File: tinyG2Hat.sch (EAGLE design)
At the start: 31 parts

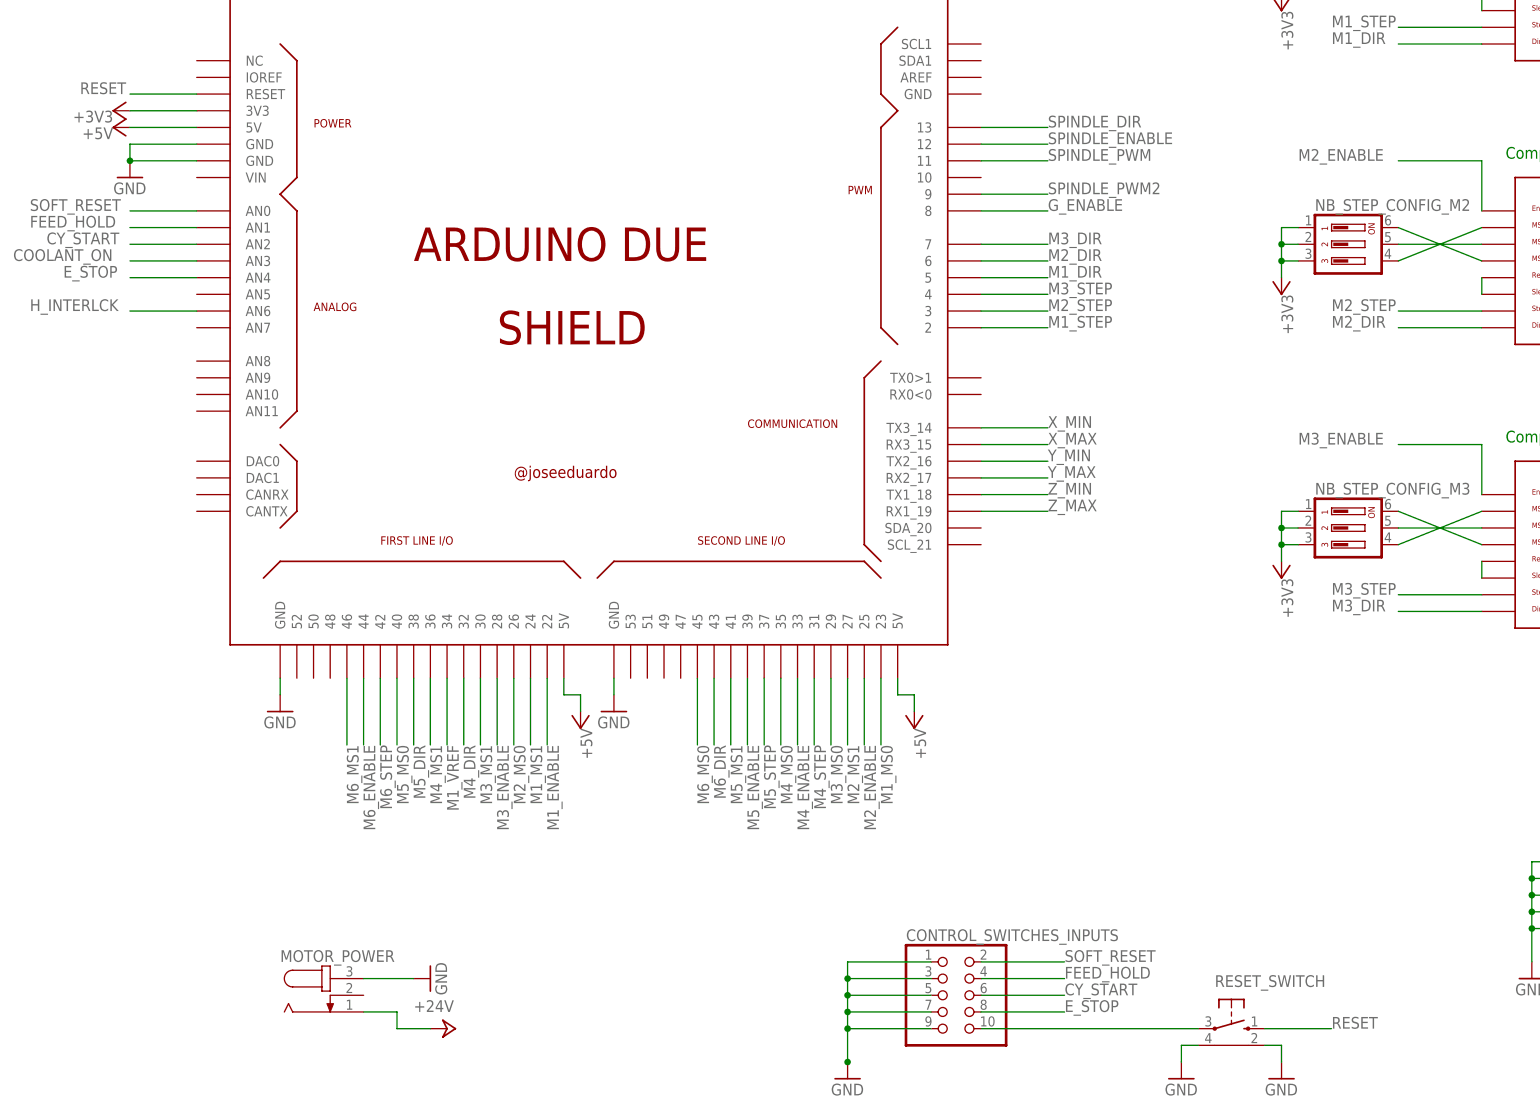
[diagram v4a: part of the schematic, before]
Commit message: Routage de base terminé
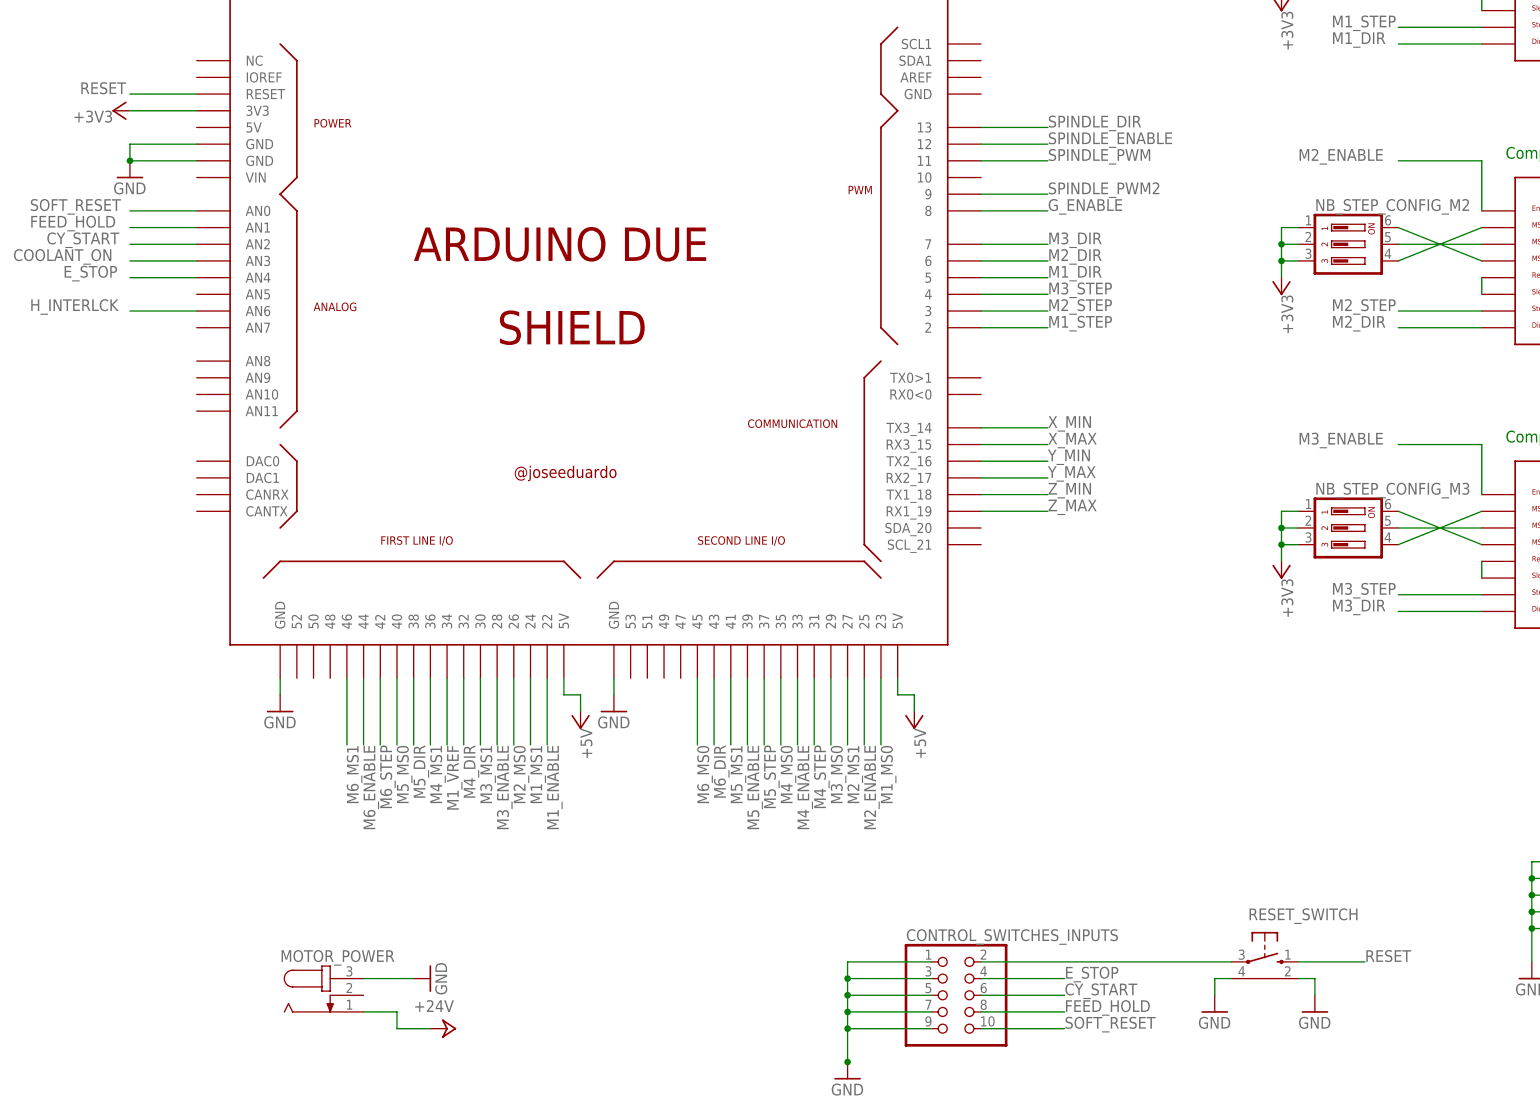
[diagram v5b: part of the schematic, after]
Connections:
- net +5V: no longer ARDUINO_DUE1.5V
- net E_STOP: now also CONTROL_SWITCHES_INPUTS.4; no longer CONTROL_SWITCHES_INPUTS.8
- net FEED_HOLD: now also CONTROL_SWITCHES_INPUTS.8; no longer CONTROL_SWITCHES_INPUTS.4
- net N$50: now also CONTROL_SWITCHES_INPUTS.2; no longer CONTROL_SWITCHES_INPUTS.10
- net SOFT_RESET: now also CONTROL_SWITCHES_INPUTS.10; no longer CONTROL_SWITCHES_INPUTS.2
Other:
- moved on the sheet: RESET_SWITCH
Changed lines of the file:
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@@
 <part name="ARDUINO_DUE1" library="arduino_due_shield" deviceset="ARDUINO_DUE_SHIELD_NOSPI" device=""/>
 <part name="+3V1" library="supply1" library_urn="urn:adsk.eagle:library:371" deviceset="+3V3" device=""/>
-<part name="P+1" library="supply1" library_urn="urn:adsk.eagle:library:371" deviceset="+5V" device=""/>
 <part name="GND1" library="supply1" library_urn="urn:adsk.eagle:library:371" deviceset="GND" device=""/>
 <part name="P+2" library="supply1" library_urn="urn:adsk.eagle:library:371" deviceset="+5V" device=""/>
@@
 <instance part="+3V1" gate="G$1" x="38.1" y="111.76" smashed="yes" rot="R90">
 <attribute name="VALUE" x="38.1" y="111.76" size="1.778" layer="96" rot="R180"/>
-</instance>
-<instance part="P+1" gate="1" x="38.1" y="109.22" smashed="yes" rot="R90">
-<attribute name="VALUE" x="38.1" y="109.22" size="1.778" layer="96" rot="R180"/>
 </instance>
 <instance part="GND1" gate="1" x="40.64" y="101.6"/>
@@
 <instance part="CONTROL_SWITCHES_INPUTS" gate="A" x="165.1" y="-22.86"/>
 <instance part="GND13" gate="1" x="149.86" y="-35.56"/>
-<instance part="RESET_SWITCH" gate="1" x="208.28" y="-27.94" rot="R270"/>
-<instance part="GND14" gate="1" x="200.66" y="-35.56"/>
-<instance part="GND15" gate="1" x="215.9" y="-35.56"/>
+<instance part="RESET_SWITCH" gate="1" x="213.36" y="-17.78" rot="R270"/>
+<instance part="GND14" gate="1" x="205.74" y="-25.4"/>
+<instance part="GND15" gate="1" x="220.98" y="-25.4"/>
 </instances>
 <busses>
@@
 </net>
 <net name="+5V" class="0">
-<segment>
-<pinref part="ARDUINO_DUE1" gate="G$1" pin="5V"/>
-<pinref part="P+1" gate="1" pin="+5V"/>
-<wire x1="40.64" y1="109.22" x2="50.8" y2="109.22" width="0.1524" layer="91"/>
-</segment>
 <segment>
 <pinref part="ARDUINO_DUE1" gate="G$1" pin="5V@1"/>
@@
 <segment>
 <pinref part="RESET_SWITCH" gate="1" pin="GND2"/>
-<wire x1="203.2" y1="-30.48" x2="200.66" y2="-30.48" width="0.1524" layer="91"/>
+<wire x1="208.28" y1="-20.32" x2="205.74" y2="-20.32" width="0.1524" layer="91"/>
 <pinref part="GND14" gate="1" pin="GND"/>
-<wire x1="200.66" y1="-30.48" x2="200.66" y2="-33.02" width="0.1524" layer="91"/>
+<wire x1="205.74" y1="-20.32" x2="205.74" y2="-22.86" width="0.1524" layer="91"/>
 </segment>
 <segment>
 <pinref part="RESET_SWITCH" gate="1" pin="GND1"/>
-<wire x1="213.36" y1="-30.48" x2="215.9" y2="-30.48" width="0.1524" layer="91"/>
+<wire x1="218.44" y1="-20.32" x2="220.98" y2="-20.32" width="0.1524" layer="91"/>
 <pinref part="GND15" gate="1" pin="GND"/>
-<wire x1="215.9" y1="-30.48" x2="215.9" y2="-33.02" width="0.1524" layer="91"/>
+<wire x1="220.98" y1="-20.32" x2="220.98" y2="-22.86" width="0.1524" layer="91"/>
 </segment>
 <segment>
@@
 <segment>
 <pinref part="RESET_SWITCH" gate="1" pin="S"/>
-<wire x1="213.36" y1="-27.94" x2="223.52" y2="-27.94" width="0.1524" layer="91"/>
-<label x="223.52" y="-27.94" size="1.778" layer="95"/>
+<wire x1="218.44" y1="-17.78" x2="228.6" y2="-17.78" width="0.1524" layer="91"/>
+<label x="228.6" y="-17.78" size="1.778" layer="95"/>
 </segment>
 </net>
@@
 </segment>
 <segment>
-<pinref part="CONTROL_SWITCHES_INPUTS" gate="A" pin="2"/>
-<wire x1="170.18" y1="-17.78" x2="182.88" y2="-17.78" width="0.1524" layer="91"/>
-<label x="182.88" y="-17.78" size="1.778" layer="95"/>
+<pinref part="CONTROL_SWITCHES_INPUTS" gate="A" pin="10"/>
+<wire x1="170.18" y1="-27.94" x2="182.88" y2="-27.94" width="0.1524" layer="91"/>
+<label x="182.88" y="-27.94" size="1.778" layer="95"/>
 </segment>
 </net>
@@
 </segment>
 <segment>
-<pinref part="CONTROL_SWITCHES_INPUTS" gate="A" pin="8"/>
-<wire x1="170.18" y1="-25.4" x2="182.88" y2="-25.4" width="0.1524" layer="91"/>
-<label x="182.88" y="-25.4" size="1.778" layer="95"/>
+<pinref part="CONTROL_SWITCHES_INPUTS" gate="A" pin="4"/>
+<wire x1="170.18" y1="-20.32" x2="182.88" y2="-20.32" width="0.1524" layer="91"/>
+<label x="182.88" y="-20.32" size="1.778" layer="95"/>
 </segment>
 </net>
@@
 <net name="FEED_HOLD" class="0">
 <segment>
-<pinref part="CONTROL_SWITCHES_INPUTS" gate="A" pin="4"/>
-<wire x1="170.18" y1="-20.32" x2="182.88" y2="-20.32" width="0.1524" layer="91"/>
-<label x="182.88" y="-20.32" size="1.778" layer="95"/>
-</segment>
-<segment>
 <pinref part="ARDUINO_DUE1" gate="G$1" pin="AN1"/>
 <wire x1="50.8" y1="93.98" x2="40.64" y2="93.98" width="0.1524" layer="91"/>
 <label x="25.4" y="93.98" size="1.778" layer="95"/>
 </segment>
+<segment>
+<pinref part="CONTROL_SWITCHES_INPUTS" gate="A" pin="8"/>
+<wire x1="170.18" y1="-25.4" x2="182.88" y2="-25.4" width="0.1524" layer="91"/>
+<label x="182.88" y="-25.4" size="1.778" layer="95"/>
+</segment>
 </net>
 <net name="N$50" class="0">
 <segment>
-<pinref part="CONTROL_SWITCHES_INPUTS" gate="A" pin="10"/>
+<pinref part="CONTROL_SWITCHES_INPUTS" gate="A" pin="2"/>
 <pinref part="RESET_SWITCH" gate="1" pin="P"/>
-<wire x1="170.18" y1="-27.94" x2="203.2" y2="-27.94" width="0.1524" layer="91"/>
-</segment>
-</net>
+<wire x1="170.18" y1="-17.78" x2="208.28" y2="-17.78" width="0.1524" layer="91"/>
+</segment>
+</net>

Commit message: Début de la sérigraphie
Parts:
- SPINDLE_OUTPUTS: device con-lstb:MA05-2 -> pinhead:PINHD-2X5
- SV1: device con-lstb:MA04-2 -> pinhead:PINHD-2X4
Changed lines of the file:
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@@
 <part name="M6" library="pinhead" library_urn="urn:adsk.eagle:library:325" deviceset="PINHD-1X4" device="" package3d_urn="urn:adsk.eagle:package:22407/2"/>
 <part name="C6" library="rcl" library_urn="urn:adsk.eagle:library:334" deviceset="CPOL-EU" device="E3.5-8" package3d_urn="urn:adsk.eagle:package:23360/2" value="100µF"/>
-<part name="SPINDLE_OUTPUTS" library="con-lstb" library_urn="urn:adsk.eagle:library:162" deviceset="MA05-2" device="" package3d_urn="urn:adsk.eagle:package:8329/1"/>
+<part name="SPINDLE_OUTPUTS" library="pinhead" library_urn="urn:adsk.eagle:library:325" deviceset="PINHD-2X5" device="" package3d_urn="urn:adsk.eagle:package:22470/2"/>
 <part name="GND11" library="supply1" library_urn="urn:adsk.eagle:library:371" deviceset="GND" device=""/>
-<part name="SV1" library="con-lstb" library_urn="urn:adsk.eagle:library:162" deviceset="MA04-2" device="" package3d_urn="urn:adsk.eagle:package:8368/1"/>
+<part name="SV1" library="pinhead" library_urn="urn:adsk.eagle:library:325" deviceset="PINHD-2X4" device="" package3d_urn="urn:adsk.eagle:package:22461/2"/>
 <part name="GND12" library="supply1" library_urn="urn:adsk.eagle:library:371" deviceset="GND" device=""/>
 <part name="S2" library="switch-dil" library_urn="urn:adsk.eagle:library:375" deviceset="DP08" device="" package3d_urn="urn:adsk.eagle:package:27224/2"/>
@@
 <instance part="M6" gate="A" x="441.96" y="43.18"/>
 <instance part="C6" gate="G$1" x="426.72" y="55.88"/>
-<instance part="SPINDLE_OUTPUTS" gate="G$1" x="266.7" y="-7.62"/>
+<instance part="SPINDLE_OUTPUTS" gate="A" x="266.7" y="-7.62" rot="R180"/>
 <instance part="GND11" gate="1" x="254" y="-20.32"/>
-<instance part="SV1" gate="G$1" x="353.06" y="-2.54"/>
+<instance part="SV1" gate="A" x="353.06" y="-2.54" rot="R180"/>
 <instance part="GND12" gate="1" x="340.36" y="-17.78"/>
 <instance part="S2" gate="1" x="386.08" y="-5.08" rot="R270"/>
@@
 </segment>
 <segment>
-<pinref part="SPINDLE_OUTPUTS" gate="G$1" pin="3"/>
-<wire x1="274.32" y1="-10.16" x2="281.94" y2="-10.16" width="0.1524" layer="91"/>
+<pinref part="SPINDLE_OUTPUTS" gate="A" pin="3"/>
+<wire x1="269.24" y1="-10.16" x2="281.94" y2="-10.16" width="0.1524" layer="91"/>
 <label x="281.94" y="-10.16" size="1.778" layer="95"/>
 </segment>
@@
 </segment>
 <segment>
-<pinref part="SPINDLE_OUTPUTS" gate="G$1" pin="5"/>
-<wire x1="274.32" y1="-7.62" x2="281.94" y2="-7.62" width="0.1524" layer="91"/>
+<pinref part="SPINDLE_OUTPUTS" gate="A" pin="5"/>
+<wire x1="269.24" y1="-7.62" x2="281.94" y2="-7.62" width="0.1524" layer="91"/>
 <label x="281.94" y="-7.62" size="1.778" layer="95"/>
 </segment>
@@
 </segment>
 <segment>
-<pinref part="SPINDLE_OUTPUTS" gate="G$1" pin="9"/>
-<wire x1="274.32" y1="-2.54" x2="281.94" y2="-2.54" width="0.1524" layer="91"/>
+<pinref part="SPINDLE_OUTPUTS" gate="A" pin="9"/>
+<wire x1="269.24" y1="-2.54" x2="281.94" y2="-2.54" width="0.1524" layer="91"/>
 <label x="281.94" y="-2.54" size="1.778" layer="95"/>
 </segment>
@@
 </segment>
 <segment>
-<pinref part="SPINDLE_OUTPUTS" gate="G$1" pin="7"/>
-<wire x1="274.32" y1="-5.08" x2="281.94" y2="-5.08" width="0.1524" layer="91"/>
+<pinref part="SPINDLE_OUTPUTS" gate="A" pin="7"/>
+<wire x1="269.24" y1="-5.08" x2="281.94" y2="-5.08" width="0.1524" layer="91"/>
 <label x="281.94" y="-5.08" size="1.778" layer="95"/>
 </segment>
@@
 </segment>
 <segment>
-<pinref part="SPINDLE_OUTPUTS" gate="G$1" pin="10"/>
-<wire x1="259.08" y1="-2.54" x2="254" y2="-2.54" width="0.1524" layer="91"/>
+<pinref part="SPINDLE_OUTPUTS" gate="A" pin="10"/>
+<wire x1="261.62" y1="-2.54" x2="254" y2="-2.54" width="0.1524" layer="91"/>
 <wire x1="254" y1="-2.54" x2="254" y2="-5.08" width="0.1524" layer="91"/>
-<pinref part="SPINDLE_OUTPUTS" gate="G$1" pin="8"/>
+<pinref part="SPINDLE_OUTPUTS" gate="A" pin="8"/>
 <wire x1="254" y1="-5.08" x2="254" y2="-7.62" width="0.1524" layer="91"/>
 <wire x1="254" y1="-7.62" x2="254" y2="-10.16" width="0.1524" layer="91"/>
 <wire x1="254" y1="-10.16" x2="254" y2="-12.7" width="0.1524" layer="91"/>
-<wire x1="259.08" y1="-5.08" x2="254" y2="-5.08" width="0.1524" layer="91"/>
+<wire x1="261.62" y1="-5.08" x2="254" y2="-5.08" width="0.1524" layer="91"/>
 <junction x="254" y="-5.08"/>
-<pinref part="SPINDLE_OUTPUTS" gate="G$1" pin="6"/>
-<wire x1="259.08" y1="-7.62" x2="254" y2="-7.62" width="0.1524" layer="91"/>
+<pinref part="SPINDLE_OUTPUTS" gate="A" pin="6"/>
+<wire x1="261.62" y1="-7.62" x2="254" y2="-7.62" width="0.1524" layer="91"/>
 <junction x="254" y="-7.62"/>
-<pinref part="SPINDLE_OUTPUTS" gate="G$1" pin="4"/>
-<wire x1="259.08" y1="-10.16" x2="254" y2="-10.16" width="0.1524" layer="91"/>
+<pinref part="SPINDLE_OUTPUTS" gate="A" pin="4"/>
+<wire x1="261.62" y1="-10.16" x2="254" y2="-10.16" width="0.1524" layer="91"/>
 <junction x="254" y="-10.16"/>
-<pinref part="SPINDLE_OUTPUTS" gate="G$1" pin="2"/>
-<wire x1="259.08" y1="-12.7" x2="254" y2="-12.7" width="0.1524" layer="91"/>
+<pinref part="SPINDLE_OUTPUTS" gate="A" pin="2"/>
+<wire x1="261.62" y1="-12.7" x2="254" y2="-12.7" width="0.1524" layer="91"/>
 <junction x="254" y="-12.7"/>
 <pinref part="GND11" gate="1" pin="GND"/>
@@
 </segment>
 <segment>
-<pinref part="SV1" gate="G$1" pin="8"/>
-<wire x1="345.44" y1="0" x2="340.36" y2="0" width="0.1524" layer="91"/>
+<pinref part="SV1" gate="A" pin="8"/>
+<wire x1="347.98" y1="0" x2="340.36" y2="0" width="0.1524" layer="91"/>
 <wire x1="340.36" y1="0" x2="340.36" y2="-2.54" width="0.1524" layer="91"/>
-<pinref part="SV1" gate="G$1" pin="6"/>
+<pinref part="SV1" gate="A" pin="6"/>
 <wire x1="340.36" y1="-2.54" x2="340.36" y2="-5.08" width="0.1524" layer="91"/>
 <wire x1="340.36" y1="-5.08" x2="340.36" y2="-7.62" width="0.1524" layer="91"/>
 <wire x1="340.36" y1="-7.62" x2="340.36" y2="-15.24" width="0.1524" layer="91"/>
-<wire x1="345.44" y1="-2.54" x2="340.36" y2="-2.54" width="0.1524" layer="91"/>
+<wire x1="347.98" y1="-2.54" x2="340.36" y2="-2.54" width="0.1524" layer="91"/>
 <junction x="340.36" y="-2.54"/>
-<pinref part="SV1" gate="G$1" pin="4"/>
-<wire x1="345.44" y1="-5.08" x2="340.36" y2="-5.08" width="0.1524" layer="91"/>
+<pinref part="SV1" gate="A" pin="4"/>
+<wire x1="347.98" y1="-5.08" x2="340.36" y2="-5.08" width="0.1524" layer="91"/>
 <junction x="340.36" y="-5.08"/>
-<pinref part="SV1" gate="G$1" pin="2"/>
-<wire x1="345.44" y1="-7.62" x2="340.36" y2="-7.62" width="0.1524" layer="91"/>
+<pinref part="SV1" gate="A" pin="2"/>
+<wire x1="347.98" y1="-7.62" x2="340.36" y2="-7.62" width="0.1524" layer="91"/>
 <junction x="340.36" y="-7.62"/>
 <pinref part="GND12" gate="1" pin="GND"/>
@@
 <net name="COOLANT_ON" class="0">
 <segment>
-<pinref part="SPINDLE_OUTPUTS" gate="G$1" pin="1"/>
-<wire x1="274.32" y1="-12.7" x2="281.94" y2="-12.7" width="0.1524" layer="91"/>
+<pinref part="SPINDLE_OUTPUTS" gate="A" pin="1"/>
+<wire x1="269.24" y1="-12.7" x2="281.94" y2="-12.7" width="0.1524" layer="91"/>
 <label x="281.94" y="-12.7" size="1.778" layer="95"/>
 </segment>
@@
 <net name="N$49" class="0">
 <segment>
-<pinref part="SV1" gate="G$1" pin="7"/>
+<pinref part="SV1" gate="A" pin="7"/>
 <pinref part="S2" gate="1" pin="1"/>
-<wire x1="360.68" y1="0" x2="360.68" y2="5.08" width="0.1524" layer="91"/>
+<wire x1="355.6" y1="0" x2="360.68" y2="5.08" width="0.1524" layer="91"/>
 <wire x1="360.68" y1="5.08" x2="375.92" y2="5.08" width="0.1524" layer="91"/>
 <pinref part="S2" gate="1" pin="2"/>
@@
 <net name="N$51" class="0">
 <segment>
-<pinref part="SV1" gate="G$1" pin="5"/>
-<wire x1="360.68" y1="-2.54" x2="363.22" y2="-2.54" width="0.1524" layer="91"/>
+<pinref part="SV1" gate="A" pin="5"/>
+<wire x1="355.6" y1="-2.54" x2="363.22" y2="-2.54" width="0.1524" layer="91"/>
 <wire x1="363.22" y1="-2.54" x2="363.22" y2="0" width="0.1524" layer="91"/>
 <pinref part="S2" gate="1" pin="3"/>
@@
 <net name="N$53" class="0">
 <segment>
-<pinref part="SV1" gate="G$1" pin="3"/>
+<pinref part="SV1" gate="A" pin="3"/>
 <pinref part="S2" gate="1" pin="5"/>
-<wire x1="360.68" y1="-5.08" x2="375.92" y2="-5.08" width="0.1524" layer="91"/>
+<wire x1="355.6" y1="-5.08" x2="375.92" y2="-5.08" width="0.1524" layer="91"/>
 <pinref part="S2" gate="1" pin="6"/>
 <wire x1="375.92" y1="-5.08" x2="378.46" y2="-5.08" width="0.1524" layer="91"/>
@@
 <net name="N$55" class="0">
 <segment>
-<pinref part="SV1" gate="G$1" pin="1"/>
-<wire x1="360.68" y1="-7.62" x2="360.68" y2="-10.16" width="0.1524" layer="91"/>
+<pinref part="SV1" gate="A" pin="1"/>
+<wire x1="355.6" y1="-7.62" x2="360.68" y2="-10.16" width="0.1524" layer="91"/>
 <pinref part="S2" gate="1" pin="7"/>
 <wire x1="360.68" y1="-10.16" x2="375.92" y2="-10.16" width="0.1524" layer="91"/>
